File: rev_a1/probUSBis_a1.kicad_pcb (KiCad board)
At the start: 2 copper layers, 44.5 x 22.9 mm, 26 parts, among them CON1 USB-MINI-B, IC1 ATTINY85-P, P1 USB_A_MALE, P2 CONN_8, P3 CONN_4, U1 LM78L05ACZ

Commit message: generating files
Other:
- board size 44.5 x 22.9 mm -> 44.5 x 23.4 mm
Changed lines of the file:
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@@
     (links 52)
     (no_connects 1)
-    (area 96.528499 90.0028 152.40127 114.59845)
+    (area 96.528499 90.0028 152.38476 114.929)
     (thickness 1.6)
-    (drawings 41)
+    (drawings 42)
     (tracks 183)
     (zones 0)
@@
   (page A4)
   (layers
-    (15 F.Cu signal hide)
-    (0 B.Cu signal hide)
+    (15 F.Cu signal)
+    (0 B.Cu signal)
     (16 B.Adhes user)
     (17 F.Adhes user)
@@
     (visible_elements FFFFFF7F)
     (pcbplotparams
-      (layerselection 3178497)
+      (layerselection 284196865)
       (usegerberextensions true)
       (excludeedgelayer true)
@@
       (xy 4.572 0.45466) (xy 4.572 0.46736) (xy 4.572 1.0922) (xy 4.572 1.0922)) (layer B.SilkS) (width 0.00254))
   )
+  (gr_line (start 149.86 114.808) (end 149.86 114.3) (angle 90) (layer Edge.Cuts) (width 0.1))
   (gr_text "Open Source\nHardware" (at 115.57 107.95 90) (layer B.SilkS)
     (effects (font (size 0.8 0.8) (thickness 0.2)) (justify mirror))
   )
-  (gr_line (start 105.41 114.3) (end 105.41 91.44) (angle 90) (layer Edge.Cuts) (width 0.1))
-  (gr_line (start 149.86 114.3) (end 105.41 114.3) (angle 90) (layer Edge.Cuts) (width 0.1))
+  (gr_line (start 105.41 114.808) (end 105.41 91.44) (angle 90) (layer Edge.Cuts) (width 0.1))
+  (gr_line (start 149.86 114.808) (end 105.41 114.808) (angle 90) (layer Edge.Cuts) (width 0.1))
   (gr_line (start 149.86 91.44) (end 149.86 114.3) (angle 90) (layer Edge.Cuts) (width 0.1))
   (gr_line (start 105.41 91.44) (end 149.86 91.44) (angle 90) (layer Edge.Cuts) (width 0.1))

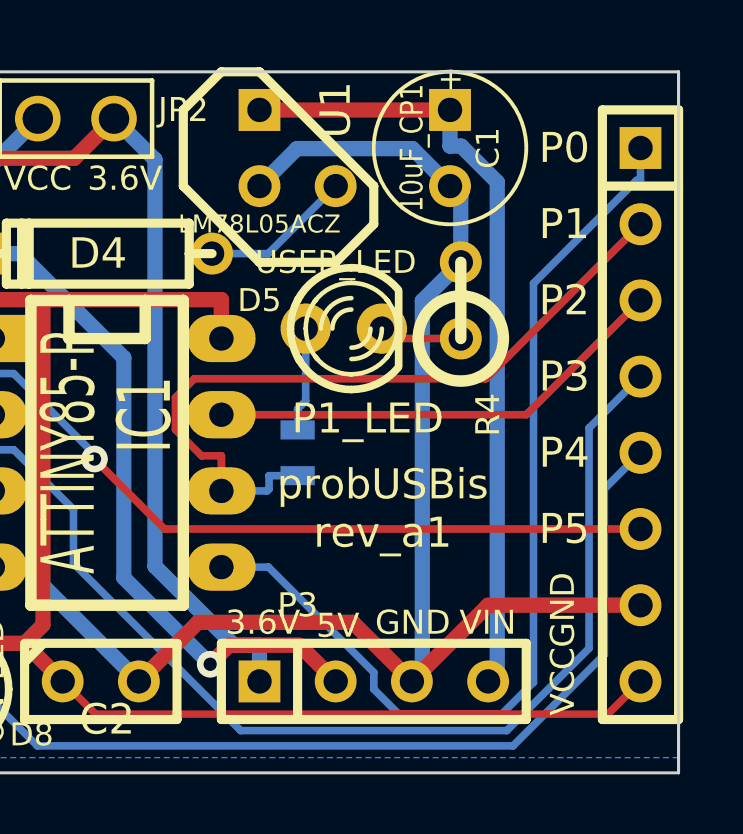
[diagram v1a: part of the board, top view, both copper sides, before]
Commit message: made some holes bigger, and made new pin modules to do so.
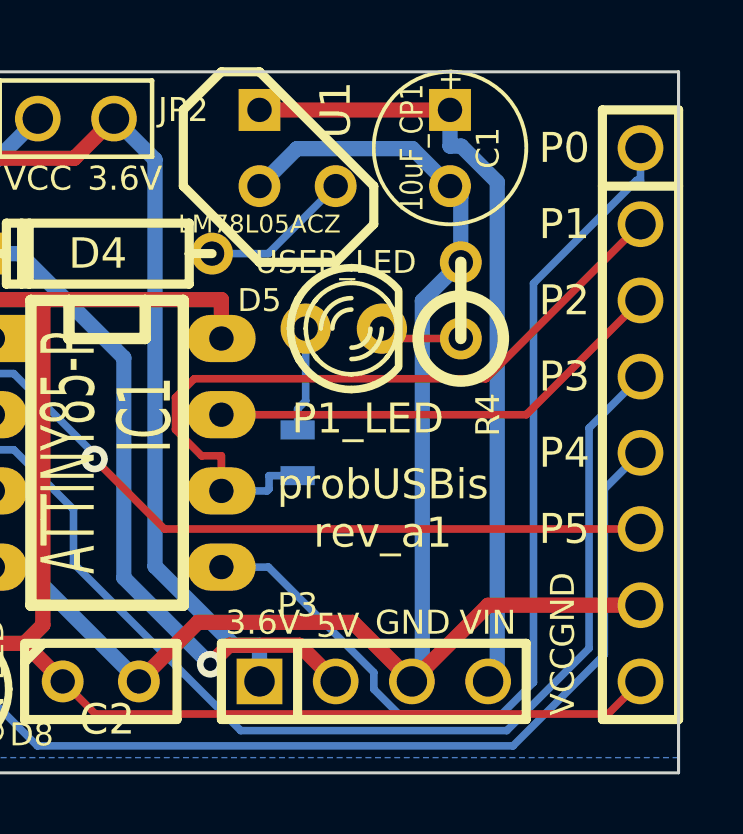
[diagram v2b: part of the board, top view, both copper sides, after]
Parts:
- P2: footprint SIL-8 -> pin8x1
- P3: footprint SIL-4 -> pin4x1
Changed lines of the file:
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@@
     (mod_text_size 1 1)
     (mod_text_width 0.15)
-    (pad_size 1.5 1.5)
-    (pad_drill 0.6)
+    (pad_size 1.524 1.524)
+    (pad_drill 1.016)
     (pad_to_mask_clearance 0)
     (aux_axis_origin 0 0)
@@
       (scale (xyz 1 1 1))
       (rotate (xyz 0 0 0))
-    )
-  )
-  (module SIL-8 (layer F.Cu)
-    (at 148.59 102.87 270)
-    (descr "Connecteur 8 pins")
-    (tags "CONN DEV")
-    (fp_text reference P2 (at -6.35 -2.54 270) (layer F.SilkS) hide
-      (effects (font (size 1.72974 1.08712) (thickness 0.27178)))
-    )
-    (fp_text value CONN_8 (at 11.43 1 360) (layer F.SilkS) hide
-      (effects (font (size 0.6 0.6) (thickness 0.15)))
-    )
-    (fp_line (start -10.16 -1.27) (end 10.16 -1.27) (layer F.SilkS) (width 0.3048))
-    (fp_line (start 10.16 -1.27) (end 10.16 1.27) (layer F.SilkS) (width 0.3048))
-    (fp_line (start 10.16 1.27) (end -10.16 1.27) (layer F.SilkS) (width 0.3048))
-    (fp_line (start -10.16 1.27) (end -10.16 -1.27) (layer F.SilkS) (width 0.3048))
-    (fp_line (start -7.62 1.27) (end -7.62 -1.27) (layer F.SilkS) (width 0.3048))
-    (pad 1 thru_hole rect (at -8.89 0 270) (size 1.397 1.397) (drill 0.8128)
-      (layers *.Cu *.Mask F.SilkS)
-      (net 15 N-000006)
-    )
-    (pad 2 thru_hole circle (at -6.35 0 270) (size 1.397 1.397) (drill 0.8128)
-      (layers *.Cu *.Mask F.SilkS)
-      (net 16 N-000007)
-    )
-    (pad 3 thru_hole circle (at -3.81 0 270) (size 1.397 1.397) (drill 0.8128)
-      (layers *.Cu *.Mask F.SilkS)
-      (net 17 N-000008)
-    )
-    (pad 4 thru_hole circle (at -1.27 0 270) (size 1.397 1.397) (drill 0.8128)
-      (layers *.Cu *.Mask F.SilkS)
-      (net 13 N-0000020)
-    )
-    (pad 5 thru_hole circle (at 1.27 0 270) (size 1.397 1.397) (drill 0.8128)
-      (layers *.Cu *.Mask F.SilkS)
-      (net 7 N-0000015)
-    )
-    (pad 6 thru_hole circle (at 3.81 0 270) (size 1.397 1.397) (drill 0.8128)
-      (layers *.Cu *.Mask F.SilkS)
-      (net 12 N-000002)
-    )
-    (pad 7 thru_hole circle (at 6.35 0 270) (size 1.397 1.397) (drill 0.8128)
-      (layers *.Cu *.Mask F.SilkS)
-      (net 3 GND)
-    )
-    (pad 8 thru_hole circle (at 8.89 0 270) (size 1.397 1.397) (drill 0.8128)
-      (layers *.Cu *.Mask F.SilkS)
-      (net 19 VCC)
-    )
-  )
-  (module SIL-4 (layer F.Cu)
-    (at 139.7 111.76)
-    (descr "Connecteur 4 pibs")
-    (tags "CONN DEV")
-    (fp_text reference P3 (at -2.54 -2.54) (layer F.SilkS)
-      (effects (font (size 0.8 0.8) (thickness 0.2)))
-    )
-    (fp_text value CONN_4 (at 0 -2.54) (layer F.SilkS) hide
-      (effects (font (size 1.524 1.016) (thickness 0.3048)))
-    )
-    (fp_line (start -5.08 -1.27) (end -5.08 -1.27) (layer F.SilkS) (width 0.3048))
-    (fp_line (start -5.08 1.27) (end -5.08 -1.27) (layer F.SilkS) (width 0.3048))
-    (fp_line (start -5.08 -1.27) (end -5.08 -1.27) (layer F.SilkS) (width 0.3048))
-    (fp_line (start -5.08 -1.27) (end 5.08 -1.27) (layer F.SilkS) (width 0.3048))
-    (fp_line (start 5.08 -1.27) (end 5.08 1.27) (layer F.SilkS) (width 0.3048))
-    (fp_line (start 5.08 1.27) (end -5.08 1.27) (layer F.SilkS) (width 0.3048))
-    (fp_line (start -2.54 1.27) (end -2.54 -1.27) (layer F.SilkS) (width 0.3048))
-    (pad 1 thru_hole rect (at -3.81 0) (size 1.397 1.397) (drill 0.8128)
-      (layers *.Cu *.Mask F.SilkS)
-      (net 1 +3.3V)
-    )
-    (pad 2 thru_hole circle (at -1.27 0) (size 1.397 1.397) (drill 0.8128)
-      (layers *.Cu *.Mask F.SilkS)
-      (net 2 +5V)
-    )
-    (pad 3 thru_hole circle (at 1.27 0) (size 1.397 1.397) (drill 0.8128)
-      (layers *.Cu *.Mask F.SilkS)
-      (net 3 GND)
-    )
-    (pad 4 thru_hole circle (at 3.81 0) (size 1.397 1.397) (drill 0.8128)
-      (layers *.Cu *.Mask F.SilkS)
-      (net 20 VIN)
     )
   )
@@
       (xy 4.572 0.45466) (xy 4.572 0.46736) (xy 4.572 1.0922) (xy 4.572 1.0922)) (layer B.SilkS) (width 0.00254))
   )
+  (module pin8x1 (layer F.Cu)
+    (at 148.59 102.87 270)
+    (descr "Connecteur 8 pins")
+    (tags "CONN DEV")
+    (fp_text reference P2 (at -6.35 -2.54 270) (layer F.SilkS) hide
+      (effects (font (size 1.72974 1.08712) (thickness 0.27178)))
+    )
+    (fp_text value CONN_8 (at 11.43 1 360) (layer F.SilkS) hide
+      (effects (font (size 0.6 0.6) (thickness 0.15)))
+    )
+    (fp_line (start -10.16 -1.27) (end 10.16 -1.27) (layer F.SilkS) (width 0.3048))
+    (fp_line (start 10.16 -1.27) (end 10.16 1.27) (layer F.SilkS) (width 0.3048))
+    (fp_line (start 10.16 1.27) (end -10.16 1.27) (layer F.SilkS) (width 0.3048))
+    (fp_line (start -10.16 1.27) (end -10.16 -1.27) (layer F.SilkS) (width 0.3048))
+    (fp_line (start -7.62 1.27) (end -7.62 -1.27) (layer F.SilkS) (width 0.3048))
+    (pad 1 thru_hole circle (at -8.89 0 270) (size 1.524 1.524) (drill 1.016)
+      (layers *.Cu *.Mask F.SilkS)
+      (net 15 N-000006)
+    )
+    (pad 2 thru_hole circle (at -6.35 0 270) (size 1.524 1.524) (drill 1.016)
+      (layers *.Cu *.Mask F.SilkS)
+      (net 16 N-000007)
+    )
+    (pad 3 thru_hole circle (at -3.81 0 270) (size 1.524 1.524) (drill 1.016)
+      (layers *.Cu *.Mask F.SilkS)
+      (net 17 N-000008)
+    )
+    (pad 4 thru_hole circle (at -1.27 0 270) (size 1.524 1.524) (drill 1.016)
+      (layers *.Cu *.Mask F.SilkS)
+      (net 13 N-0000020)
+    )
+    (pad 5 thru_hole circle (at 1.27 0 270) (size 1.524 1.524) (drill 1.016)
+      (layers *.Cu *.Mask F.SilkS)
+      (net 7 N-0000015)
+    )
+    (pad 6 thru_hole circle (at 3.81 0 270) (size 1.524 1.524) (drill 1.016)
+      (layers *.Cu *.Mask F.SilkS)
+      (net 12 N-000002)
+    )
+    (pad 7 thru_hole circle (at 6.35 0 270) (size 1.524 1.524) (drill 1.016)
+      (layers *.Cu *.Mask F.SilkS)
+      (net 3 GND)
+    )
+    (pad 8 thru_hole circle (at 8.89 0 270) (size 1.524 1.524) (drill 1.016)
+      (layers *.Cu *.Mask F.SilkS)
+      (net 19 VCC)
+    )
+  )
+  (module pin4x1 (layer F.Cu)
+    (at 139.7 111.76)
+    (descr "Connecteur 4 pibs")
+    (tags "CONN DEV")
+    (fp_text reference P3 (at -2.54 -2.54) (layer F.SilkS)
+      (effects (font (size 0.8 0.8) (thickness 0.2)))
+    )
+    (fp_text value CONN_4 (at 0 -2.54) (layer F.SilkS) hide
+      (effects (font (size 1.524 1.016) (thickness 0.3048)))
+    )
+    (fp_line (start -5.08 -1.27) (end -5.08 -1.27) (layer F.SilkS) (width 0.3048))
+    (fp_line (start -5.08 1.27) (end -5.08 -1.27) (layer F.SilkS) (width 0.3048))
+    (fp_line (start -5.08 -1.27) (end -5.08 -1.27) (layer F.SilkS) (width 0.3048))
+    (fp_line (start -5.08 -1.27) (end 5.08 -1.27) (layer F.SilkS) (width 0.3048))
+    (fp_line (start 5.08 -1.27) (end 5.08 1.27) (layer F.SilkS) (width 0.3048))
+    (fp_line (start 5.08 1.27) (end -5.08 1.27) (layer F.SilkS) (width 0.3048))
+    (fp_line (start -2.54 1.27) (end -2.54 -1.27) (layer F.SilkS) (width 0.3048))
+    (pad 1 thru_hole rect (at -3.81 0) (size 1.524 1.524) (drill 1.016)
+      (layers *.Cu *.Mask F.SilkS)
+      (net 1 +3.3V)
+    )
+    (pad 2 thru_hole circle (at -1.27 0) (size 1.524 1.524) (drill 1.016)
+      (layers *.Cu *.Mask F.SilkS)
+      (net 2 +5V)
+    )
+    (pad 3 thru_hole circle (at 1.27 0) (size 1.524 1.524) (drill 1.016)
+      (layers *.Cu *.Mask F.SilkS)
+      (net 3 GND)
+    )
+    (pad 4 thru_hole circle (at 3.81 0) (size 1.524 1.524) (drill 1.016)
+      (layers *.Cu *.Mask F.SilkS)
+      (net 20 VIN)
+    )
+  )
   (gr_line (start 149.86 114.808) (end 149.86 114.3) (angle 90) (layer Edge.Cuts) (width 0.1))
